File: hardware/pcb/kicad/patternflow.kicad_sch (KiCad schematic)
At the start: 35 parts, among them J1 Conn_02x08_Odd_Even, J2 Screw_Terminal_01x02, J3 Screw_Terminal_01x02, SW1 RotaryEncoder_Switch, SW2 RotaryEncoder_Switch, SW3 RotaryEncoder_Switch, SW4 RotaryEncoder_Switch, U1 ESP32-S3-DevKit-44pin

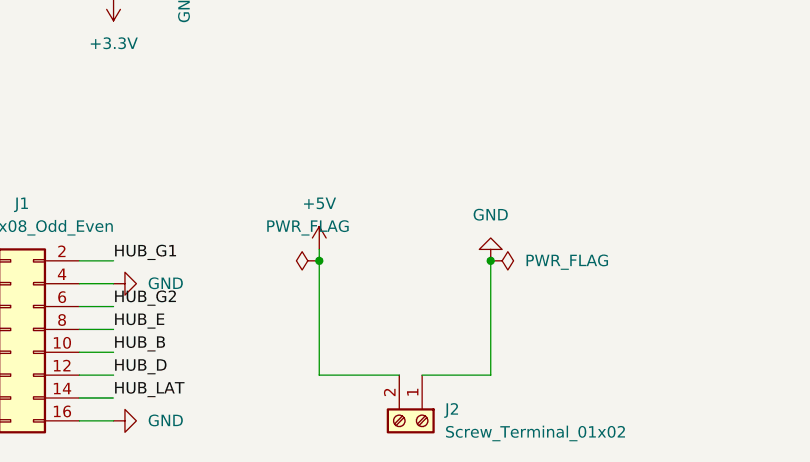
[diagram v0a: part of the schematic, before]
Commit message: hardware: update PCB gerbers to v2
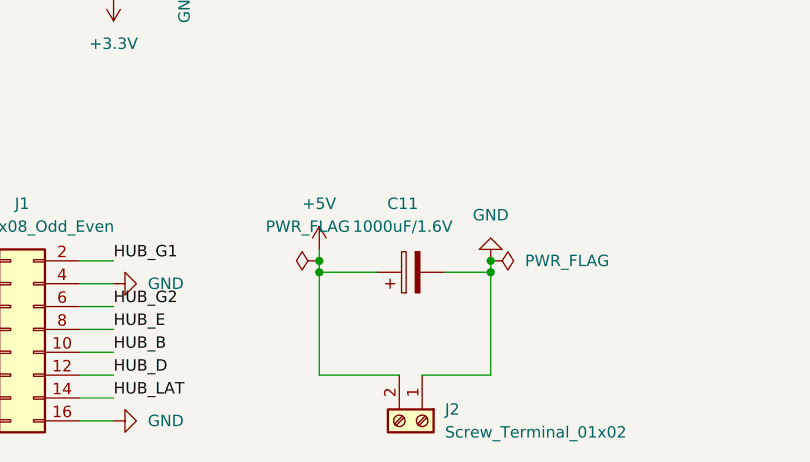
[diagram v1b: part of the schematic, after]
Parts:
- added C11: 1000uF/1.6V, Capacitor_THT:CP_Radial_D10.0mm_P5.00mm, symbol Device:C_Polarized
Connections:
- net +5V: now also C11.1
- net GND: now also C11.2
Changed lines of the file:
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@@
 	)
 	(junction
+		(at 146.05 165.1)
+		(diameter 0)
+		(color 0 0 0 0)
+	)
+	(junction
 		(at 34.29 124.46)
 		(diameter 0)
@@
 	)
 	(junction
+		(at 127 165.1)
+		(diameter 0)
+		(color 0 0 0 0)
+	)
+	(junction
 		(at 41.91 124.46)
 		(diameter 0)
@@
 	(wire
 		(pts
+			(xy 140.97 165.1) (xy 146.05 165.1)
+		)
+		(stroke
+			(width 0)
+			(type default)
+		)
+	)
+	(wire
+		(pts
 			(xy 38.1 64.77) (xy 40.64 64.77)
 		)
@@
 	(wire
 		(pts
-			(xy 146.05 163.83) (xy 146.05 176.53)
+			(xy 146.05 163.83) (xy 146.05 165.1)
 		)
 		(stroke
@@
 	(wire
 		(pts
+			(xy 127 165.1) (xy 127 176.53)
+		)
+		(stroke
+			(width 0)
+			(type default)
+		)
+	)
+	(wire
+		(pts
 			(xy 104.14 114.3) (xy 104.14 116.84)
 		)
@@
 	(wire
 		(pts
-			(xy 127 163.83) (xy 127 176.53)
+			(xy 127 163.83) (xy 127 165.1)
 		)
 		(stroke
@@
 	(wire
 		(pts
+			(xy 146.05 165.1) (xy 146.05 176.53)
+		)
+		(stroke
+			(width 0)
+			(type default)
+		)
+	)
+	(wire
+		(pts
 			(xy 129.54 121.92) (xy 129.54 133.35)
 		)
@@
 	(wire
 		(pts
+			(xy 127 165.1) (xy 133.35 165.1)
+		)
+		(stroke
+			(width 0)
+			(type default)
+		)
+	)
+	(wire
+		(pts
 			(xy 30.48 64.77) (xy 38.1 64.77)
 		)
@@
 					(unit 1)
 				)
+			)
+		)
+	)
+	(symbol
+		(lib_id "Device:C_Polarized")
+		(at 137.16 165.1 90)
+		(unit 1)
+		(body_style 1)
+		(exclude_from_sim no)
+		(in_bom yes)
+		(on_board yes)
+		(in_pos_files yes)
+		(dnp no)
+		(fields_autoplaced yes)
+		(property "Reference" "C11"
+			(at 136.271 157.48 90)
+			(show_name no)
+			(do_not_autoplace no)
+			(effects
+				(font
+					(size 1.27 1.27)
+				)
+			)
+		)
+		(property "Value" "1000uF/1.6V"
+			(at 136.271 160.02 90)
+			(show_name no)
+			(do_not_autoplace no)
+			(effects
+				(font
+					(size 1.27 1.27)
+				)
+			)
+		)
+		(property "Footprint" "Capacitor_THT:CP_Radial_D10.0mm_P5.00mm"
+			(at 140.97 164.1348 0)
+			(hide yes)
+			(show_name no)
+			(do_not_autoplace no)
+			(effects
+				(font
+					(size 1.27 1.27)
+				)
+			)
+		)
+		(property "Datasheet" ""
+			(at 137.16 165.1 0)
+			(hide yes)
+			(show_name no)
+			(do_not_autoplace no)
+			(effects
+				(font
+					(size 1.27 1.27)
+				)
+			)
+		)
+		(property "Description" "Polarized capacitor"
+			(at 137.16 165.1 0)
+			(hide yes)
+			(show_name no)
+			(do_not_autoplace no)
+			(effects
+				(font
+					(size 1.27 1.27)
+				)
+			)
+		)
+		(pin "1"
+		)
+		(pin "2"
+		)
+		(instances
+			(project "patternflow"
+				(path "/7829ca74-397b-4e20-b2ed-d34479de16a0"
+					(reference "C11")
+					(unit 1)
+				)
